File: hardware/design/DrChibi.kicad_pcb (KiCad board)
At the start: 4 copper layers, 143.5 x 14 mm, 237 parts, among them P1 CONN_02X05, P2 PAD_SMD, P3 IN+, P4 IN-, P5 CONN_01X04, U1 STM32F40X_LQFP64, U2 ISO1050, X1 MINI-USB-SHIELD-32005-201, X2 8MHz 10ppm

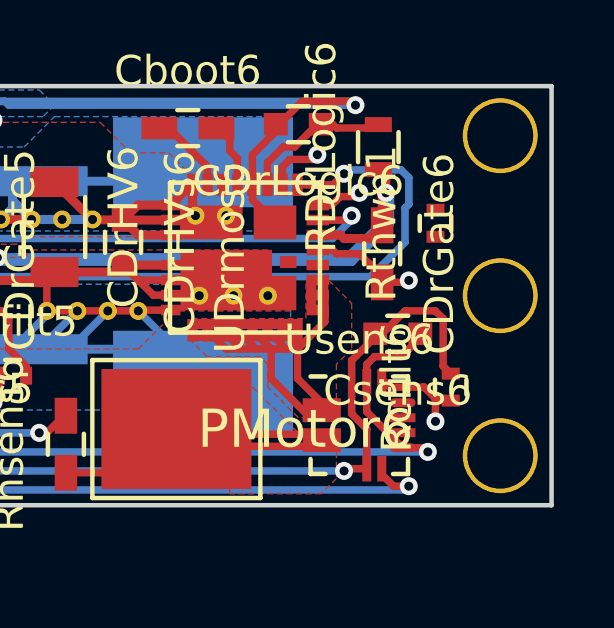
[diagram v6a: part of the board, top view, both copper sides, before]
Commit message: Added pullup resistor for THWn.
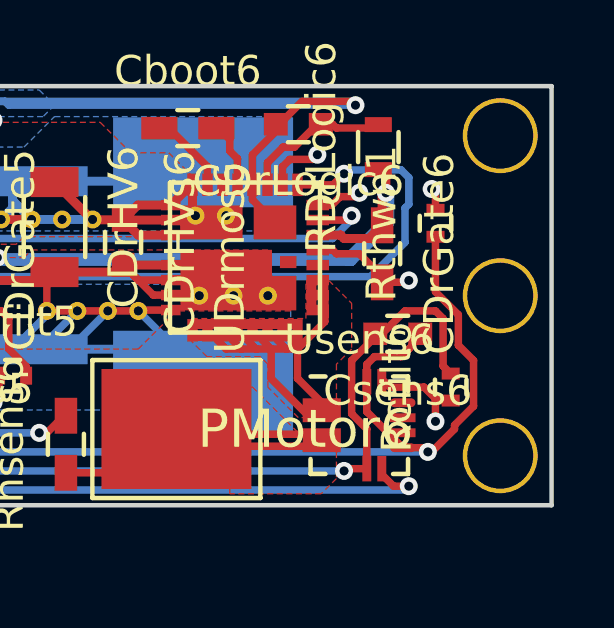
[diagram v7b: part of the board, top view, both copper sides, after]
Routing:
- net +3V3: track 229.8 -> 238.2 mm
- net /Half Bridge A/THWn: track 106.4 -> 110.2 mm, vias 7 -> 8
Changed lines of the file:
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@@
-(kicad_pcb (version 4) (host pcbnew "(2016-02-29 BZR 6600)-product")
+(kicad_pcb (version 4) (host pcbnew 4.1.0-alpha+201607160317+6981~46~ubuntu16.04.1-product)
   (general
     (links 600)
-    (no_connects 3)
-    (area 34.424999 92.939999 178.075001 107.060001)
+    (no_connects 1)
+    (area 23.501026 88.629166 180.752095 113.328971)
     (thickness 1.6)
     (drawings 31)
-    (tracks 3554)
+    (tracks 3568)
     (zones 0)
     (modules 237)
@@
   (layers
     (0 F.Cu signal)
-    (1 In1.Cu mixed hide)
-    (2 In2.Cu mixed hide)
+    (1 In1.Cu mixed)
+    (2 In2.Cu mixed)
     (31 B.Cu signal)
     (33 F.Adhes user)
@@
   (module CRF1:1PAD_4x5mm (layer F.Cu)
     (at 91.834 104.445 270)
-    (fp_text reference PMotor1 (at 0 -4.3 540) (layer F.SilkS)
+    (fp_text reference PMotor1 (at 0 -4.3 180) (layer F.SilkS)
       (effects (font (thickness 0.3048)))
     )
@@
   (module CRF1:1PAD_4x5mm (layer F.Cu)
     (at 106.566 104.445 270)
-    (fp_text reference PMotor2 (at 0 -4.3 540) (layer F.SilkS)
+    (fp_text reference PMotor2 (at 0 -4.3 180) (layer F.SilkS)
       (effects (font (thickness 0.3048)))
     )
@@
   (module CRF1:1PAD_4x5mm (layer F.Cu)
     (at 121.425 104.445 270)
-    (fp_text reference PMotor3 (at 0 -4.3 540) (layer F.SilkS)
+    (fp_text reference PMotor3 (at 0 -4.3 180) (layer F.SilkS)
       (effects (font (thickness 0.3048)))
     )
@@
   (module CRF1:1PAD_4x5mm (layer F.Cu)
     (at 136.157 104.445 270)
-    (fp_text reference PMotor4 (at 0 -4.3 540) (layer F.SilkS)
+    (fp_text reference PMotor4 (at 0 -4.3 180) (layer F.SilkS)
       (effects (font (thickness 0.3048)))
     )
@@
   (module CRF1:1PAD_4x5mm (layer F.Cu)
     (at 150.762 104.445 270)
-    (fp_text reference PMotor5 (at 0 -4.3 540) (layer F.SilkS)
+    (fp_text reference PMotor5 (at 0 -4.3 180) (layer F.SilkS)
       (effects (font (thickness 0.3048)))
     )
@@
   (module CRF1:1PAD_4x5mm (layer F.Cu)
     (at 165.494 104.445 270)
-    (fp_text reference PMotor6 (at 0 -4.3 540) (layer F.SilkS)
+    (fp_text reference PMotor6 (at 0 -4.3 180) (layer F.SilkS)
       (effects (font (thickness 0.3048)))
     )
@@
     (at 166.383 95.555 270)
     (descr Pad)
-    (fp_text reference P3 (at 0 4.8 360) (layer B.SilkS)
+    (fp_text reference P3 (at 0 4.8) (layer B.SilkS)
       (effects (font (thickness 0.3048)) (justify mirror))
     )
@@
     (at 166.383 102.921 270)
     (descr Pad)
-    (fp_text reference P4 (at 0 4.8 360) (layer B.SilkS)
+    (fp_text reference P4 (at 0 4.8) (layer B.SilkS)
       (effects (font (thickness 0.3048)) (justify mirror))
     )
@@
   (segment (start 59.31 96.317) (end 61.0185 96.317) (width 0.25) (layer F.Cu) (net 3))
   (segment (start 61.0185 96.317) (end 61.039 96.3375) (width 0.25) (layer F.Cu) (net 3))
+  (segment (start 174.13 98.037) (end 174.13 99.873) (width 0.25) (layer F.Cu) (net 4) (status 400000))
+  (segment (start 174.003 105.207) (end 173.876 105.207) (width 0.25) (layer F.Cu) (net 4))
+  (segment (start 174.765 104.445) (end 174.003 105.207) (width 0.25) (layer F.Cu) (net 4))
+  (segment (start 174.765 104.318) (end 174.765 104.445) (width 0.25) (layer F.Cu) (net 4))
+  (segment (start 175.4 103.683) (end 174.765 104.318) (width 0.25) (layer F.Cu) (net 4))
+  (segment (start 175.4 102.159) (end 175.4 103.683) (width 0.25) (layer F.Cu) (net 4))
+  (segment (start 174.892 101.651) (end 175.4 102.159) (width 0.25) (layer F.Cu) (net 4))
+  (segment (start 174.892 100.635) (end 174.892 101.651) (width 0.25) (layer F.Cu) (net 4))
+  (segment (start 174.13 99.873) (end 174.892 100.635) (width 0.25) (layer F.Cu) (net 4))
   (segment (start 48.781 97.206) (end 49.67 96.317) (width 0.25) (layer In1.Cu) (net 4))
   (segment (start 49.67 96.317) (end 57.417 96.317) (width 0.25) (layer In1.Cu) (net 4))
@@
   (segment (start 96.545 96.98) (end 96.632 96.98) (width 0.25) (layer F.Cu) (net 41))
   (segment (start 96.545 96.98) (end 96.759 96.98) (width 0.25) (layer F.Cu) (net 41))
+  (segment (start 174.13 97.137) (end 174.13 96.571) (width 0.25) (layer F.Cu) (net 42) (status 400000))
+  (segment (start 173.114 97.333) (end 171.336 97.333) (width 0.25) (layer In1.Cu) (net 42))
+  (segment (start 174.003 96.444) (end 173.114 97.333) (width 0.25) (layer In1.Cu) (net 42))
+  (via (at 174.003 96.444) (size 0.6) (drill 0.3) (layers F.Cu B.Cu) (net 42))
+  (segment (start 174.13 96.571) (end 174.003 96.444) (width 0.25) (layer F.Cu) (net 42))
   (segment (start 171.336 97.333) (end 171.336 97.46) (width 0.25) (layer B.Cu) (net 42))
   (segment (start 157.239 98.095) (end 170.701 98.095) (width 0.25) (layer B.Cu) (net 42))

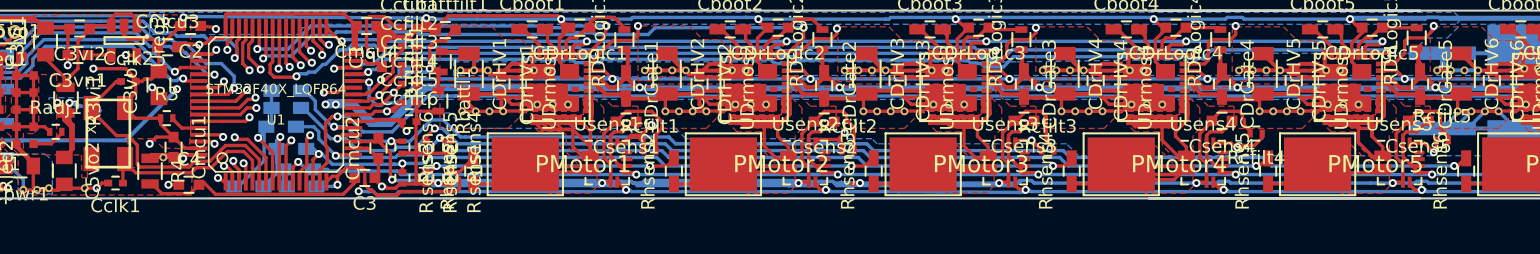
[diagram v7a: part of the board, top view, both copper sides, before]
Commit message: Fixed Crystal pin 4 not connected to GND
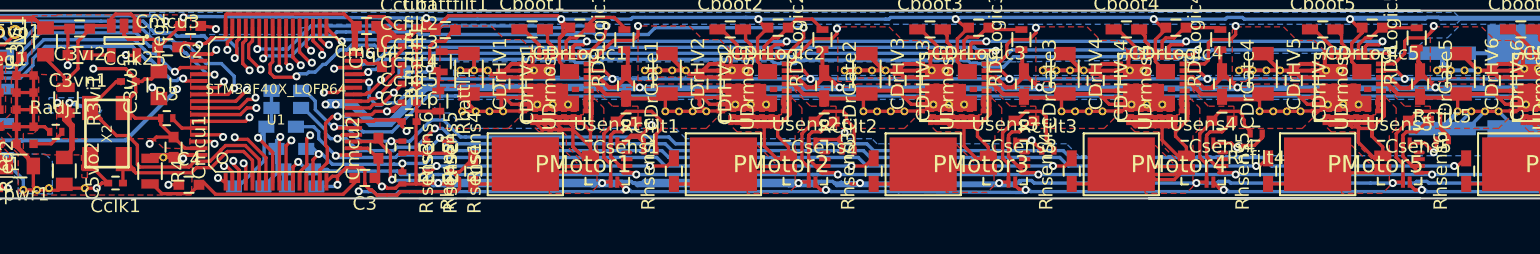
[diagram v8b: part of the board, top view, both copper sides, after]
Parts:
- Ccfilt1, Ccfilt2, Ccfilt3, Ccfilt4, Ccfilt5, Ccfilt6: value C -> 0.5n
- Rcfilt1, Rcfilt2, Rcfilt3, Rcfilt4, Rcfilt5, Rcfilt6: value R -> 20k
- X2: footprint CRF1:Crystal_5x3mm -> Crystals_User:Crystal_5x3mm
- moved X2 0.10 mm to (60.7, 102.2)
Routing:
- net GND: track 943.0 -> 949.2 mm
- net Net-(Cclk2-Pad1): track 21.3 -> 22.5 mm
- net Net-(Cclk1-Pad1): track 14.6 -> 15.8 mm
